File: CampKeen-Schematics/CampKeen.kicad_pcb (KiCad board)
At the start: 4 copper layers, 193.7 x 142.2 mm, 304 parts, among them IC1 CD74HC4050ME4, IC2 LM2597MX-ADJ_NOPB, IC3 LM2670SX-5.0_NOPB, IC4 DS3231SN#, IC5 OPA2340PA, IC6 OPA2340PA, J1 Vin, J10 Conn_01x19, J11 Conn_01x19, J2 Conn_01x02, J3 CircuitSetupsSplitPhase, J4 Conn_01x02, J5 Conn_01x02, J6 Conn_01x02, J7 GenEnclosure, J8 GenHeadL, J9 GenHeadR, P1 Power, P10 CONN_01X01, P11 CONN_01X01, P12 CONN_01X01, P13 CONN_01X01, P2 Analog, P3 Analog, P4 Digital, P5 PWM, P6 PWM, P7 Communication, P8 CONN_01X01, P9 CONN_01X01, Q1 IRF9Z34NPBF, Q10 2N7000, Q11 IRF9Z34NPBF, Q12 2N7000, Q13 2N7000, Q14 2N7000, Q15 2N7000, Q16 2N7000, Q17 2N7000, Q18 2N7000, Q19 2N7000, Q2 2N7000, Q20 LTV-847, Q21 2N7000, Q22 2N7000, Q23 2N7000, Q24 2N7000, Q25 LTV-847, Q26 2N7000, Q27 2N7000, Q28 2N7000, Q29 2N7000, Q3 IRF9Z34NPBF, Q30 2N7000, Q31 2N7000, Q32 IRF9Z34NPBF, Q33 IRF9Z34NPBF, Q34 2N7000, Q35 IRF9Z34NPBF, Q36 2N7000, Q37 IRF9Z34NPBF, Q38 2N7000, Q39 IRF9Z34NPBF, Q4 2N7000, Q40 2N7000, Q41 IRF9Z34NPBF, Q42 2N7000, Q43 2N7000, Q44 IRF9Z34NPBF, Q45 IRF9Z34NPBF, Q46 2N7000, Q47 IRF9Z34NPBF, Q48 2N7000, Q49 IRF9Z34NPBF, Q5 2N7000, Q50 2N7000, Q51 IRF9Z34NPBF, Q52 2N7000, Q53 IRF9Z34NPBF, Q54 LTV-847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

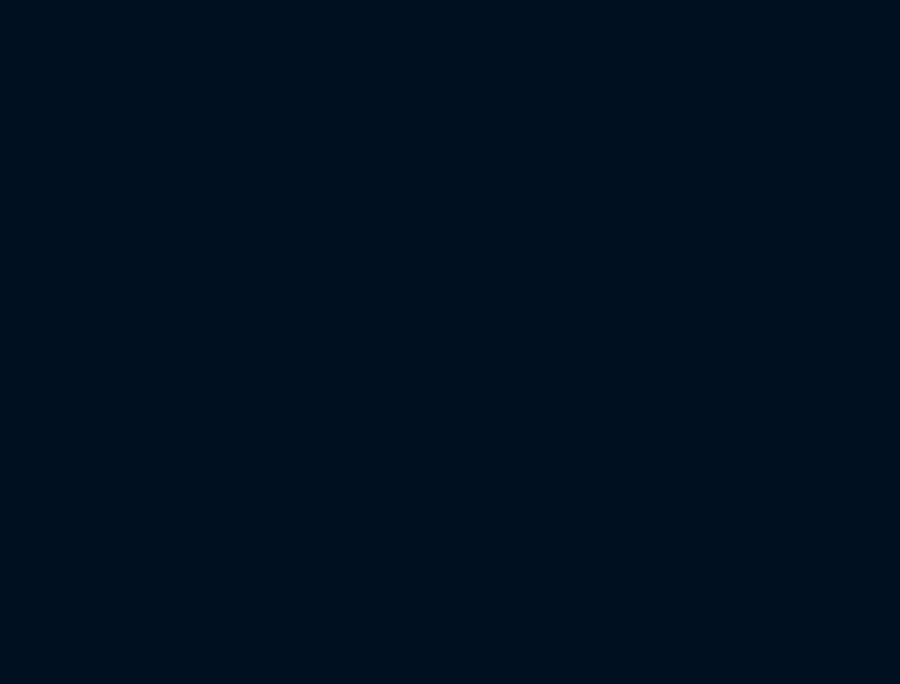
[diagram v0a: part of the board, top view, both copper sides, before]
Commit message: working on getting the board cleaned enough to start placing the new designs and chips.
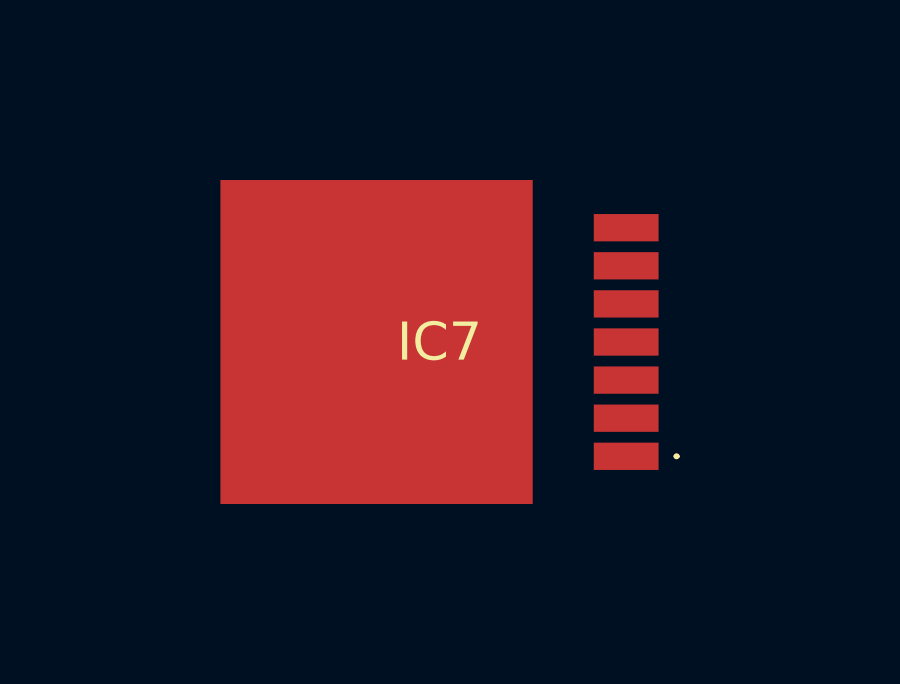
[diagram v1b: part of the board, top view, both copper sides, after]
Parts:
- added IC7: LM2670SX-3.3_NOPB, SamacSys_Parts:LM2670SX33NOPB, F.Cu at (157.7, 65.5)
- C28: value 120uF -> 180uF
- L3: value 33uH -> 22uH
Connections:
- C27 pad 1: unconnected-(C27-Pad1) -> Net-(C27-Pad1)
- R14 pad 2: unconnected-(R14-Pad2) -> Net-(R14-Pad2)
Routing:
- net Net-(Q17-Pad3): track 0.00 -> 5.00 mm
- net IO41: track 5.00 -> 0.00 mm
- net Net-(Q19-Pad3): track 0.00 -> 4.23 mm
- net IO26: track 4.23 -> 0.00 mm
- net Net-(Q18-Pad3): track 0.00 -> 3.86 mm
- net IO29: track 3.86 -> 0.00 mm

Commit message: wip for placement of components and I2c Buffer
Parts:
- added IC8: P82B715TD,112, SamacSys_Parts:SOIC127P600X175-8N, F.Cu at (149.3, 13.3)
- added RV4: 500k, Potentiometer_THT:Potentiometer_Bourns_3296W_Vertical, F.Cu at (115.1, 32.7)
- added RV5: 500k, Potentiometer_THT:Potentiometer_Bourns_3296W_Vertical, F.Cu at (132.8, 24.8)
- moved D3 275.0 mm to (119.5, -15.7), turned to 0 degrees
- moved D6 268.5 mm to (133.4, -20.0), turned to 0 degrees
- moved Q4 267.4 mm to (119.6, -4.56), turned to 0 degrees
- moved C16 264.5 mm to (117.8, 5.29)
- moved IC1 261.2 mm to (130.0, 15.8), turned to 0 degrees
- moved R20 259.9 mm to (153.8, -20.1)
- moved C18 259.3 mm to (109.1, 5.29)
- moved R18 259.0 mm to (135.6, -2.03), turned to 0 degrees
- moved Q58 258.9 mm to (112.3, -11.2), turned to 0 degrees
- moved Q5 258.8 mm to (126.1, -4.56), turned to 0 degrees
- moved Q6 258.3 mm to (126.1, -10.3), turned to 0 degrees
- moved C17 257.0 mm to (123.1, 5.02)
- moved R19 256.8 mm to (145.1, -10.5), turned to 0 degrees
- moved D8 256.1 mm to (108.8, 1.91), turned to 0 degrees
- moved R17 255.0 mm to (139.7, -15.8)
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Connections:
- net A2 renamed IO11
- IO4 pad 3: SDA -> IO43
- IO4 pad 6: SCL -> IO46
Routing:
- net GND: track 209.7 -> 277.8 mm, vias 1 -> 0
- net +3V3: track 0.00 -> 41.2 mm, vias 0 -> 1
- net Net-(5VOut1-Pad1): track 90.6 -> 60.8 mm
- net +12V: track 476.7 -> 452.5 mm, vias 1 -> 2
- net Net-(C27-Pad2): track 0.00 -> 19.0 mm
- net +BATT: track 193.0 -> 180.2 mm
- net Net-(IC7-Pad5): track 0.00 -> 6.67 mm
- net Net-(C27-Pad1): track 0.00 -> 4.39 mm
- net Net-(Q19-Pad3): track 4.23 -> 0.00 mm
- net GreyV: track 4.16 -> 0.00 mm
- net Net-(Q18-Pad3): track 3.86 -> 0.00 mm
- net Net-(Q17-Pad3): track 5.00 -> 1.75 mm
- net Net-(C7-Pad1): track 15.8 -> 18.8 mm
- net A7: vias 1 -> 0
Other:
- board text removed: "LCD Back"
- board text removed: "Sewage Tank"

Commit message: alright massive changes. some part switches and some reassignments. mostly it's switching out stuff for SMD so that i have more space.
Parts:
- Q10, Q2, Q30, Q31, Q34, Q36, Q38, Q40, Q42, Q43, Q46, Q48, Q50, Q52, Q56, Q8: value 2N7000 -> 2N7002; footprint Package_TO_SOT_THT:TO-92_Inline -> Package_TO_SOT_SMD:SOT-23
- moved R15 252.5 mm to (222.8, 220.4)
- moved R17 251.1 mm to (207.8, 225.9)
- moved Q2 248.1 mm to (214.9, 218.7)
- moved R16 245.6 mm to (213.3, 225.9)
- moved R40 210.6 mm to (213.3, 193.3)
- moved Q10 205.9 mm to (207.2, 192.9)
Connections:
- net AUXVoltage2 renamed CityWaterPressure
- net IO11 renamed A2
- net IO210 renamed A1
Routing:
- net Net-(5VOut1-Pad1): track 60.8 -> 40.5 mm
- net GND: track 277.8 -> 276.6 mm
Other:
- board text added: "City Water Pressure"
- board text added: "Gen Fuel Press"
- board text removed: "AUX2"
- board text removed: "AUX3"
